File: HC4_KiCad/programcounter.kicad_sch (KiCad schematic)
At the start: 3 parts, among them IC12 74HC161, IC13 74HC161, IC14 74HC161

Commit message: I'm tired. あとは任せた　頑張りたまえ
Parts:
- added CP10, CP11, CP12: 0.1u, Capacitor_THT:C_Disc_D3.0mm_W1.6mm_P2.50mm, symbol Device2:C_Bypass
- added LD10, LD11, LD12, LD13, LD14, LD15, LD16, LD17, LD6, LD7, LD8, LD9: LED, LED_THT:LED_Rectangular_W5.0mm_H2.0mm, symbol Device2:LED_
- added RN3: 1k, Resistor_THT:R_Array_SIP5, symbol Device:R_Network04_Split
- added RN4: 1k, Resistor_THT:R_Array_SIP9, symbol Device:R_Network08_Split
- renumbered IC12 to IC13, IC13 to IC14, IC14 to IC15
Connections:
- net GND: now also CP10.2, CP11.2, CP12.2, RN3.1 (R1), RN3.1 (R1), RN3.1 (R1), RN3.1 (R1), RN4.1 (R1), RN4.1 (R1), RN4.1 (R1), RN4.1 (R1), RN4.1 (R1), RN4.1 (R1), RN4.1 (R1), RN4.1 (R1)
- net PC_0: now also LD17.2
- net PC_1: now also LD14.2
- net PC_10: now also LD9.2
- net PC_11: now also LD6.2
- net PC_2: now also LD11.2
- net PC_3: now also LD8.2
- net PC_4: now also LD16.2
- net PC_5: now also LD13.2
- net PC_6: now also LD10.2
- net PC_7: now also LD7.2
- net PC_8: now also LD15.2
- net PC_9: now also LD12.2
- net VCC: now also CP10.1, CP11.1, CP12.1
- new net: LD12.1 (K), RN3.4 (R3.2)
- new net: LD16.1 (K), RN4.6 (R5.2)
- new net: LD15.1 (K), RN3.5 (R4.2)
- new net: LD10.1 (K), RN4.8 (R7.2)
- new net: LD9.1 (K), RN3.3 (R2.2)
- new net: LD6.1 (K), RN3.2 (R1.2)
- new net: LD13.1 (K), RN4.7 (R6.2)
- new net: LD14.1 (K), RN4.4 (R3.2)
- new net: LD7.1 (K), RN4.9 (R8.2)
- new net: LD17.1 (K), RN4.5 (R4.2)
- new net: LD11.1 (K), RN4.3 (R2.2)
- new net: LD8.1 (K), RN4.2 (R1.2)
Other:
- title: (none) -> CPU

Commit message: 回路図の修正
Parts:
- renumbered LD8 to LD10, LD9 to LD11, LD10 to LD12, LD11 to LD13, LD12 to LD14, LD13 to LD15, LD14 to LD16, LD15 to LD17, LD16 to LD18, LD17 to LD19, LD6 to LD8, LD7 to LD9
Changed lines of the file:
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@@
 		(on_board yes)
 		(dnp no)
-		(property "Reference" "#PWR045"
+		(property "Reference" "#PWR046"
 			(at 127 114.3 0)
 			(effects
@@
 			(project "HC4_KiCad"
 				(path "/33731ded-38c0-4297-bdd8-92b082f46ff8/7ee18210-5407-4798-af07-3cd6c855784b"
-					(reference "#PWR045")
+					(reference "#PWR046")
 					(unit 1)
 				)
@@
 		(dnp no)
 		(fields_autoplaced yes)
-		(property "Reference" "LD16"
+		(property "Reference" "LD18"
 			(at 170.18 113.3474 90)
 			(effects
@@
 			(project "HC4_KiCad"
 				(path "/33731ded-38c0-4297-bdd8-92b082f46ff8/7ee18210-5407-4798-af07-3cd6c855784b"
-					(reference "LD16")
+					(reference "LD18")
 					(unit 1)
 				)
@@
 		(dnp no)
 		(fields_autoplaced yes)
-		(property "Reference" "#PWR051"
+		(property "Reference" "#PWR052"
 			(at 142.24 176.53 0)
 			(effects
@@
 			(project ""
 				(path "/33731ded-38c0-4297-bdd8-92b082f46ff8/7ee18210-5407-4798-af07-3cd6c855784b"
-					(reference "#PWR051")
+					(reference "#PWR052")
 					(unit 1)
 				)
@@
 		(dnp no)
 		(fields_autoplaced yes)
-		(property "Reference" "LD15"
+		(property "Reference" "LD17"
 			(at 170.18 70.1674 90)
 			(effects
@@
 			(project "HC4_KiCad"
 				(path "/33731ded-38c0-4297-bdd8-92b082f46ff8/7ee18210-5407-4798-af07-3cd6c855784b"
-					(reference "LD15")
+					(reference "LD17")
 					(unit 1)
 				)
@@
 		(dnp no)
 		(fields_autoplaced yes)
-		(property "Reference" "LD10"
+		(property "Reference" "LD12"
 			(at 152.4 113.3474 90)
 			(effects
@@
 			(project "HC4_KiCad"
 				(path "/33731ded-38c0-4297-bdd8-92b082f46ff8/7ee18210-5407-4798-af07-3cd6c855784b"
-					(reference "LD10")
+					(reference "LD12")
 					(unit 1)
 				)
@@
 		(on_board yes)
 		(dnp no)
-		(property "Reference" "#PWR043"
+		(property "Reference" "#PWR044"
 			(at 127 71.12 0)
 			(effects
@@
 			(project "HC4_KiCad"
 				(path "/33731ded-38c0-4297-bdd8-92b082f46ff8/7ee18210-5407-4798-af07-3cd6c855784b"
-					(reference "#PWR043")
+					(reference "#PWR044")
 					(unit 1)
 				)
@@
 		(on_board yes)
 		(dnp no)
-		(property "Reference" "#PWR044"
+		(property "Reference" "#PWR045"
 			(at 127 78.74 0)
 			(effects
@@
 			(project "HC4_KiCad"
 				(path "/33731ded-38c0-4297-bdd8-92b082f46ff8/7ee18210-5407-4798-af07-3cd6c855784b"
-					(reference "#PWR044")
+					(reference "#PWR045")
 					(unit 1)
 				)
@@
 		(dnp no)
 		(fields_autoplaced yes)
-		(property "Reference" "LD13"
+		(property "Reference" "LD15"
 			(at 161.29 113.3474 90)
 			(effects
@@
 			(project "HC4_KiCad"
 				(path "/33731ded-38c0-4297-bdd8-92b082f46ff8/7ee18210-5407-4798-af07-3cd6c855784b"
-					(reference "LD13")
+					(reference "LD15")
 					(unit 1)
 				)
@@
 		(on_board yes)
 		(dnp no)
-		(property "Reference" "#PWR046"
+		(property "Reference" "#PWR047"
 			(at 127 121.92 0)
 			(effects
@@
 			(project "HC4_KiCad"
 				(path "/33731ded-38c0-4297-bdd8-92b082f46ff8/7ee18210-5407-4798-af07-3cd6c855784b"
-					(reference "#PWR046")
+					(reference "#PWR047")
 					(unit 1)
 				)
@@
 		(dnp no)
 		(fields_autoplaced yes)
-		(property "Reference" "LD7"
+		(property "Reference" "LD9"
 			(at 143.51 113.3474 90)
 			(effects
@@
 			(project "HC4_KiCad"
 				(path "/33731ded-38c0-4297-bdd8-92b082f46ff8/7ee18210-5407-4798-af07-3cd6c855784b"
-					(reference "LD7")
+					(reference "LD9")
 					(unit 1)
 				)
@@
 		(dnp no)
 		(fields_autoplaced yes)
-		(property "Reference" "LD6"
+		(property "Reference" "LD8"
 			(at 143.51 70.1674 90)
 			(effects
@@
 			(project "HC4_KiCad"
 				(path "/33731ded-38c0-4297-bdd8-92b082f46ff8/7ee18210-5407-4798-af07-3cd6c855784b"
-					(reference "LD6")
+					(reference "LD8")
 					(unit 1)
 				)
@@
 		(dnp no)
 		(fields_autoplaced yes)
-		(property "Reference" "#PWR050"
+		(property "Reference" "#PWR051"
 			(at 142.24 132.08 0)
 			(effects
@@
 			(project ""
 				(path "/33731ded-38c0-4297-bdd8-92b082f46ff8/7ee18210-5407-4798-af07-3cd6c855784b"
-					(reference "#PWR050")
+					(reference "#PWR051")
 					(unit 1)
 				)
@@
 		(dnp no)
 		(fields_autoplaced yes)
-		(property "Reference" "LD9"
+		(property "Reference" "LD11"
 			(at 152.4 70.1674 90)
 			(effects
@@
 			(project "HC4_KiCad"
 				(path "/33731ded-38c0-4297-bdd8-92b082f46ff8/7ee18210-5407-4798-af07-3cd6c855784b"
-					(reference "LD9")
+					(reference "LD11")
 					(unit 1)
 				)
@@
 		(dnp no)
 		(fields_autoplaced yes)
-		(property "Reference" "#PWR049"
+		(property "Reference" "#PWR050"
 			(at 142.24 88.9 0)
 			(effects
@@
 			(project ""
 				(path "/33731ded-38c0-4297-bdd8-92b082f46ff8/7ee18210-5407-4798-af07-3cd6c855784b"
-					(reference "#PWR049")
+					(reference "#PWR050")
 					(unit 1)
 				)
@@
 		(dnp no)
 		(fields_autoplaced yes)
-		(property "Reference" "#PWR047"
+		(property "Reference" "#PWR048"
 			(at 127 158.75 0)
 			(effects
@@
 			(project "HC4_KiCad"
 				(path "/33731ded-38c0-4297-bdd8-92b082f46ff8/7ee18210-5407-4798-af07-3cd6c855784b"
-					(reference "#PWR047")
+					(reference "#PWR048")
 					(unit 1)
 				)
@@
 		(dnp no)
 		(fields_autoplaced yes)
-		(property "Reference" "#PWR041"
+		(property "Reference" "#PWR042"
 			(at 124.46 176.53 0)
 			(effects
@@
 			(project ""
 				(path "/33731ded-38c0-4297-bdd8-92b082f46ff8/7ee18210-5407-4798-af07-3cd6c855784b"
-					(reference "#PWR041")
+					(reference "#PWR042")
 					(unit 1)
 				)
@@
 		(dnp no)
 		(fields_autoplaced yes)
-		(property "Reference" "LD14"
+		(property "Reference" "LD16"
 			(at 161.29 157.7974 90)
 			(effects
@@
 			(project "HC4_KiCad"
 				(path "/33731ded-38c0-4297-bdd8-92b082f46ff8/7ee18210-5407-4798-af07-3cd6c855784b"
-					(reference "LD14")
+					(reference "LD16")
 					(unit 1)
 				)
@@
 		(dnp no)
 		(fields_autoplaced yes)
-		(property "Reference" "LD8"
+		(property "Reference" "LD10"
 			(at 143.51 157.7974 90)
 			(effects
@@
 			(project "HC4_KiCad"
 				(path "/33731ded-38c0-4297-bdd8-92b082f46ff8/7ee18210-5407-4798-af07-3cd6c855784b"
-					(reference "LD8")
+					(reference "LD10")
 					(unit 1)
 				)
@@
 		(dnp no)
 		(fields_autoplaced yes)
-		(property "Reference" "LD17"
+		(property "Reference" "LD19"
 			(at 170.18 157.7974 90)
 			(effects
@@
 			(project "HC4_KiCad"
 				(path "/33731ded-38c0-4297-bdd8-92b082f46ff8/7ee18210-5407-4798-af07-3cd6c855784b"
-					(reference "LD17")
+					(reference "LD19")
 					(unit 1)
 				)
@@
 		(dnp no)
 		(fields_autoplaced yes)
-		(property "Reference" "#PWR048"
+		(property "Reference" "#PWR049"
 			(at 137.16 193.04 0)
 			(effects
@@
 			(project ""
 				(path "/33731ded-38c0-4297-bdd8-92b082f46ff8/7ee18210-5407-4798-af07-3cd6c855784b"
-					(reference "#PWR048")
+					(reference "#PWR049")
 					(unit 1)
 				)
@@
 		(dnp no)
 		(fields_autoplaced yes)
-		(property "Reference" "LD12"
+		(property "Reference" "LD14"
 			(at 161.29 70.1674 90)
 			(effects
@@
 			(project "HC4_KiCad"
 				(path "/33731ded-38c0-4297-bdd8-92b082f46ff8/7ee18210-5407-4798-af07-3cd6c855784b"
-					(reference "LD12")
+					(reference "LD14")
 					(unit 1)
 				)
@@
 		(dnp no)
 		(fields_autoplaced yes)
-		(property "Reference" "LD11"
+		(property "Reference" "LD13"
 			(at 152.4 157.7974 90)
 			(effects
@@
 			(project "HC4_KiCad"
 				(path "/33731ded-38c0-4297-bdd8-92b082f46ff8/7ee18210-5407-4798-af07-3cd6c855784b"
-					(reference "LD11")
+					(reference "LD13")
 					(unit 1)
 				)
@@
 		(on_board yes)
 		(dnp no)
-		(property "Reference" "#PWR042"
+		(property "Reference" "#PWR043"
 			(at 127 35.56 0)
 			(effects
@@
 			(project "HC4_KiCad"
 				(path "/33731ded-38c0-4297-bdd8-92b082f46ff8/7ee18210-5407-4798-af07-3cd6c855784b"
-					(reference "#PWR042")
+					(reference "#PWR043")
 					(unit 1)
 				)

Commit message: フットプリントの割り当て修正
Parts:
- IC13, IC14, IC15: footprint (none) -> Package_DIP:DIP-16_W7.62mm_Socket
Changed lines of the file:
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@@
 	(label "Level_B2"
 		(at 104.14 97.79 0)
+		(fields_autoplaced yes)
 		(effects
 			(font
@@
 	(label "Level_A0"
 		(at 107.95 147.32 0)
+		(fields_autoplaced yes)
 		(effects
 			(font
@@
 	(label "PC_3"
 		(at 149.86 139.7 0)
+		(fields_autoplaced yes)
 		(effects
 			(font
@@
 	(label "Level_C3"
 		(at 104.14 52.07 0)
+		(fields_autoplaced yes)
 		(effects
 			(font
@@
 	(label "Level_B0"
 		(at 104.14 102.87 0)
+		(fields_autoplaced yes)
 		(effects
 			(font
@@
 	(label "PC_0"
 		(at 149.86 147.32 0)
+		(fields_autoplaced yes)
 		(effects
 			(font
@@
 	(label "Level_A2"
 		(at 107.95 142.24 0)
+		(fields_autoplaced yes)
 		(effects
 			(font
@@
 	(label "PC_6"
 		(at 149.86 97.79 0)
+		(fields_autoplaced yes)
 		(effects
 			(font
@@
 	(label "PC_5"
 		(at 149.86 100.33 0)
+		(fields_autoplaced yes)
 		(effects
 			(font
@@
 	(label "PC_9"
 		(at 149.86 57.15 0)
+		(fields_autoplaced yes)
 		(effects
 			(font
@@
 	(label "Level_A1"
 		(at 107.95 144.78 0)
+		(fields_autoplaced yes)
 		(effects
 			(font
@@
 	(label "PC_1"
 		(at 149.86 144.78 0)
+		(fields_autoplaced yes)
 		(effects
 			(font
@@
 	(label "Level_B3"
 		(at 104.14 95.25 0)
+		(fields_autoplaced yes)
 		(effects
 			(font
@@
 	(label "PC_11"
 		(at 149.86 52.07 0)
+		(fields_autoplaced yes)
 		(effects
 			(font
@@
 	(label "PC_4"
 		(at 149.86 102.87 0)
+		(fields_autoplaced yes)
 		(effects
 			(font
@@
 	(label "PC_7"
 		(at 149.86 95.25 0)
+		(fields_autoplaced yes)
 		(effects
 			(font
@@
 	(label "Level_C2"
 		(at 104.14 54.61 0)
+		(fields_autoplaced yes)
 		(effects
 			(font
@@
 	(label "Level_B1"
 		(at 104.14 100.33 0)
+		(fields_autoplaced yes)
 		(effects
 			(font
@@
 	(label "PC_10"
 		(at 149.86 54.61 0)
+		(fields_autoplaced yes)
 		(effects
 			(font
@@
 	(label "Level_A3"
 		(at 107.95 139.7 0)
+		(fields_autoplaced yes)
 		(effects
 			(font
@@
 	(label "Level_C0"
 		(at 104.14 59.69 0)
+		(fields_autoplaced yes)
 		(effects
 			(font
@@
 	(label "PC_8"
 		(at 149.86 59.69 0)
+		(fields_autoplaced yes)
 		(effects
 			(font
@@
 	(label "Level_C1"
 		(at 104.14 57.15 0)
+		(fields_autoplaced yes)
 		(effects
 			(font
@@
 	(label "PC_2"
 		(at 149.86 142.24 0)
+		(fields_autoplaced yes)
 		(effects
 			(font
@@
 		(shape input)
 		(at 114.3 83.82 180)
+		(fields_autoplaced yes)
 		(effects
 			(font
@@
 		(shape input)
 		(at 102.87 134.62 180)
+		(fields_autoplaced yes)
 		(effects
 			(font
@@
 		(shape output)
 		(at 182.88 52.07 0)
+		(fields_autoplaced yes)
 		(effects
 			(font
@@
 		(shape input)
 		(at 99.06 90.17 180)
+		(fields_autoplaced yes)
 		(effects
 			(font
@@
 		(shape input)
 		(at 114.3 40.64 180)
+		(fields_autoplaced yes)
 		(effects
 			(font
@@
 		(shape input)
 		(at 99.06 46.99 180)
+		(fields_autoplaced yes)
 		(effects
 			(font
@@
 		(shape input)
 		(at 114.3 128.27 180)
+		(fields_autoplaced yes)
 		(effects
 			(font
@@
 			)
 		)
-		(property "Footprint" ""
+		(property "Footprint" "Package_DIP:DIP-16_W7.62mm_Socket"
 			(at 127 33.02 0)
 			(effects
@@
 			)
 		)
-		(property "Footprint" ""
+		(property "Footprint" "Package_DIP:DIP-16_W7.62mm_Socket"
 			(at 127 76.2 0)
 			(effects
@@
 			)
 		)
-		(property "Footprint" ""
+		(property "Footprint" "Package_DIP:DIP-16_W7.62mm_Socket"
 			(at 127 120.65 0)
 			(effects

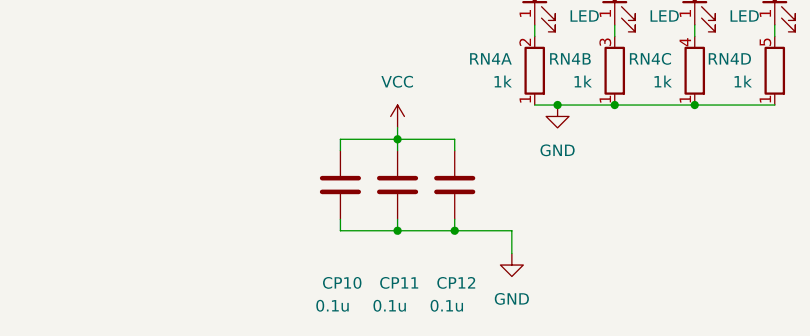
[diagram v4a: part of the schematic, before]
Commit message: ICの配置を再検討
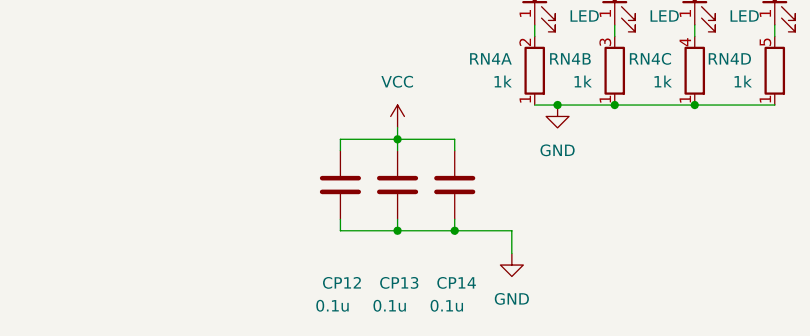
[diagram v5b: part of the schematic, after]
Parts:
- renumbered CP10 to CP12, CP11 to CP13, CP12 to CP14
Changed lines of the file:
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@@
 	(label "Level_B2"
 		(at 104.14 97.79 0)
-		(fields_autoplaced yes)
 		(effects
 			(font
@@
 	(label "Level_A0"
 		(at 107.95 147.32 0)
-		(fields_autoplaced yes)
 		(effects
 			(font
@@
 	(label "PC_3"
 		(at 149.86 139.7 0)
-		(fields_autoplaced yes)
 		(effects
 			(font
@@
 	(label "Level_C3"
 		(at 104.14 52.07 0)
-		(fields_autoplaced yes)
 		(effects
 			(font
@@
 	(label "Level_B0"
 		(at 104.14 102.87 0)
-		(fields_autoplaced yes)
 		(effects
 			(font
@@
 	(label "PC_0"
 		(at 149.86 147.32 0)
-		(fields_autoplaced yes)
 		(effects
 			(font
@@
 	(label "Level_A2"
 		(at 107.95 142.24 0)
-		(fields_autoplaced yes)
 		(effects
 			(font
@@
 	(label "PC_6"
 		(at 149.86 97.79 0)
-		(fields_autoplaced yes)
 		(effects
 			(font
@@
 	(label "PC_5"
 		(at 149.86 100.33 0)
-		(fields_autoplaced yes)
 		(effects
 			(font
@@
 	(label "PC_9"
 		(at 149.86 57.15 0)
-		(fields_autoplaced yes)
 		(effects
 			(font
@@
 	(label "Level_A1"
 		(at 107.95 144.78 0)
-		(fields_autoplaced yes)
 		(effects
 			(font
@@
 	(label "PC_1"
 		(at 149.86 144.78 0)
-		(fields_autoplaced yes)
 		(effects
 			(font
@@
 	(label "Level_B3"
 		(at 104.14 95.25 0)
-		(fields_autoplaced yes)
 		(effects
 			(font
@@
 	(label "PC_11"
 		(at 149.86 52.07 0)
-		(fields_autoplaced yes)
 		(effects
 			(font
@@
 	(label "PC_4"
 		(at 149.86 102.87 0)
-		(fields_autoplaced yes)
 		(effects
 			(font
@@
 	(label "PC_7"
 		(at 149.86 95.25 0)
-		(fields_autoplaced yes)
 		(effects
 			(font
@@
 	(label "Level_C2"
 		(at 104.14 54.61 0)
-		(fields_autoplaced yes)
 		(effects
 			(font
@@
 	(label "Level_B1"
 		(at 104.14 100.33 0)
-		(fields_autoplaced yes)
 		(effects
 			(font
@@
 	(label "PC_10"
 		(at 149.86 54.61 0)
-		(fields_autoplaced yes)
 		(effects
 			(font
@@
 	(label "Level_A3"
 		(at 107.95 139.7 0)
-		(fields_autoplaced yes)
 		(effects
 			(font
@@
 	(label "Level_C0"
 		(at 104.14 59.69 0)
-		(fields_autoplaced yes)
 		(effects
 			(font
@@
 	(label "PC_8"
 		(at 149.86 59.69 0)
-		(fields_autoplaced yes)
 		(effects
 			(font
@@
 	(label "Level_C1"
 		(at 104.14 57.15 0)
-		(fields_autoplaced yes)
 		(effects
 			(font
@@
 	(label "PC_2"
 		(at 149.86 142.24 0)
-		(fields_autoplaced yes)
 		(effects
 			(font
@@
 		(shape input)
 		(at 114.3 83.82 180)
-		(fields_autoplaced yes)
 		(effects
 			(font
@@
 		(shape input)
 		(at 102.87 134.62 180)
-		(fields_autoplaced yes)
 		(effects
 			(font
@@
 		(shape output)
 		(at 182.88 52.07 0)
-		(fields_autoplaced yes)
 		(effects
 			(font
@@
 		(shape input)
 		(at 99.06 90.17 180)
-		(fields_autoplaced yes)
 		(effects
 			(font
@@
 		(shape input)
 		(at 114.3 40.64 180)
-		(fields_autoplaced yes)
 		(effects
 			(font
@@
 		(shape input)
 		(at 99.06 46.99 180)
-		(fields_autoplaced yes)
 		(effects
 			(font
@@
 		(shape input)
 		(at 114.3 128.27 180)
-		(fields_autoplaced yes)
 		(effects
 			(font
@@
 		(on_board yes)
 		(dnp no)
-		(property "Reference" "CP11"
+		(property "Reference" "CP13"
 			(at 122.428 189.992 0)
 			(effects
@@
 			(project "HC4_KiCad"
 				(path "/33731ded-38c0-4297-bdd8-92b082f46ff8/7ee18210-5407-4798-af07-3cd6c855784b"
-					(reference "CP11")
+					(reference "CP13")
 					(unit 1)
 				)
@@
 		(on_board yes)
 		(dnp no)
-		(property "Reference" "CP12"
+		(property "Reference" "CP14"
 			(at 128.778 189.992 0)
 			(effects
@@
 			(project "HC4_KiCad"
 				(path "/33731ded-38c0-4297-bdd8-92b082f46ff8/7ee18210-5407-4798-af07-3cd6c855784b"
-					(reference "CP12")
+					(reference "CP14")
 					(unit 1)
 				)
@@
 		(on_board yes)
 		(dnp no)
-		(property "Reference" "CP10"
+		(property "Reference" "CP12"
 			(at 116.078 189.992 0)
 			(effects
@@
 			(project "HC4_KiCad"
 				(path "/33731ded-38c0-4297-bdd8-92b082f46ff8/7ee18210-5407-4798-af07-3cd6c855784b"
-					(reference "CP10")
+					(reference "CP12")
 					(unit 1)
 				)
